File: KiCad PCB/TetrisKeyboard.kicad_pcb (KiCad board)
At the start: 2 copper layers, 100 x 94 mm, 23 parts, among them SW1 SW_Cherry_MX_1.00u_PCB, SW10 SW_Cherry_MX_1.00u_PCB, SW2 SW_Cherry_MX_1.00u_PCB, SW3 SW_Cherry_MX_1.00u_PCB, SW4 SW_Cherry_MX_1.00u_PCB, SW5 SW_Cherry_MX_1.00u_PCB, SW6 SW_Cherry_MX_1.00u_PCB, SW7 SW_Cherry_MX_1.00u_PCB, SW8 SW_Cherry_MX_1.00u_PCB, SW9 SW_Cherry_MX_1.00u_PCB

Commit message: Update file structure and pcb
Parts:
- D10, D6, D7, D8, D9: moved to F.Cu
- moved D10 3.85 mm to (96.0, 119.8)
- moved D9 2.88 mm to (51.4, 105.6)
- moved D7 2.72 mm to (57.0, 105.6)
- moved D8 2.72 mm to (62.6, 105.6)
- moved D6 2.56 mm to (68.0, 105.6)
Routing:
- net Row2-B: track 231.0 -> 215.6 mm, vias 1 -> 0

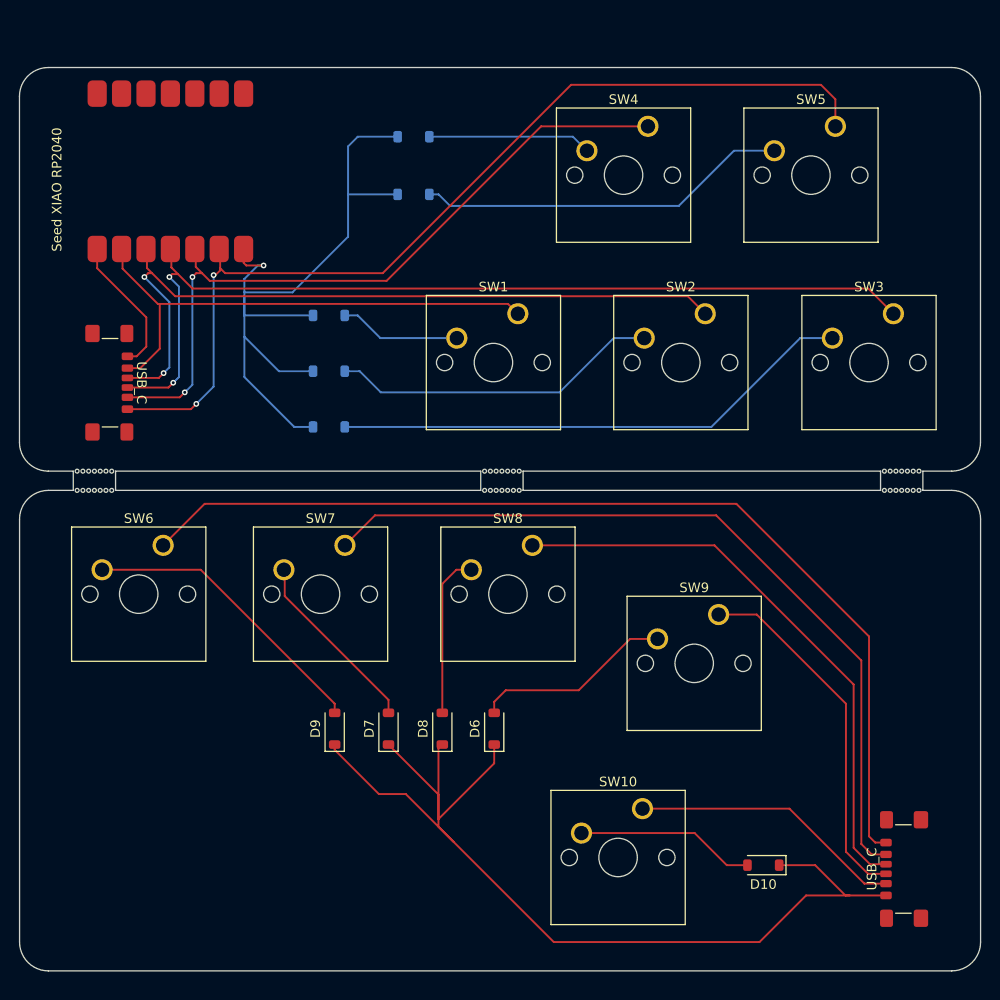
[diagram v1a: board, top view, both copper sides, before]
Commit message: Change to hot-swappable sockets, added mounting holes
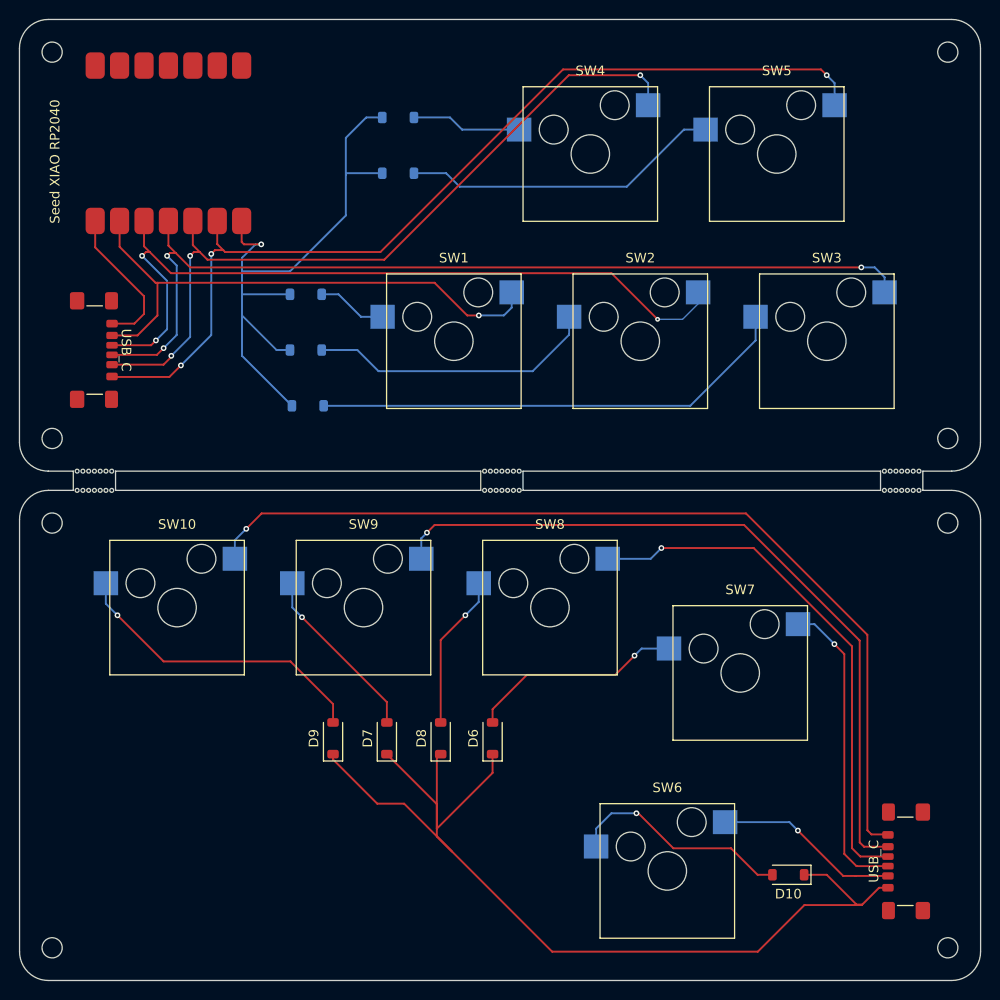
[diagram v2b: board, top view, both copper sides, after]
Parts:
- added 2.1mm: MountingHole_2.1mm, MountingHole:MountingHole_2.1mm, F.Cu at (22.0, 128.4)
- added 2.1mm: MountingHole_2.1mm, MountingHole:MountingHole_2.1mm, F.Cu at (115.2, 128.4)
- added 2.1mm: MountingHole_2.1mm, MountingHole:MountingHole_2.1mm, F.Cu at (115.2, 35.2)
- added 2.1mm: MountingHole_2.1mm, MountingHole:MountingHole_2.1mm, F.Cu at (22.0, 84.2)
- added 2.1mm: MountingHole_2.1mm, MountingHole:MountingHole_2.1mm, F.Cu at (22.0, 35.2)
- added 2.1mm: MountingHole_2.1mm, MountingHole:MountingHole_2.1mm, F.Cu at (22.0, 75.4)
- added REF**: MountingHole_2.1mm, MountingHole:MountingHole_2.1mm, F.Cu at (115.2, 84.2)
- added REF**: MountingHole_2.1mm, MountingHole:MountingHole_2.1mm, F.Cu at (115.2, 75.4)
- SW1, SW10, SW2, SW3, SW4, SW5, SW6, SW7, SW8, SW9: value SW_Cherry_MX_1.00u_PCB -> CherryMX_1.00u_KailhSocket; footprint Button_Switch_Keyboard:SW_Cherry_MX_1.00u_PCB -> CherryMX_KailhSocket:CherryMX_1.00u_KailhSocket
- moved SW6 62.5 mm to (86.0, 120.4)
- moved SW10 52.8 mm to (35.0, 93.0)
- moved SW7 43.2 mm to (93.6, 99.8)
- moved SW9 37.0 mm to (54.4, 93.0)
- moved SW3 7.50 mm to (102.6, 65.3)
- moved SW2 7.34 mm to (83.2, 65.3)
- moved SW1 7.25 mm to (63.8, 65.3)
- moved SW5 6.75 mm to (97.4, 45.8)
- moved SW8 6.73 mm to (73.8, 93.0)
- moved SW4 6.66 mm to (78.0, 45.8)
- moved USB_C 3.76 mm to (25.2, 66.2)
- moved D1 3.26 mm to (48.4, 60.4)
- moved D2 3.26 mm to (48.4, 66.2)
- moved D3 3.11 mm to (48.6, 72.0)
- moved Seed XIAO RP2040 2.92 mm to (44.6, 53.6)
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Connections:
- SW1 pad 1: Col1 -> Row1
- SW1 pad 2: Row1 -> Col1
- SW10 pad 1: Col1-B -> Row2-B
- SW10 pad 2: Row2-B -> Col5-B
- SW2 pad 1: Col2 -> Row1
- SW2 pad 2: Row1 -> Col2
- SW3 pad 1: Col3 -> Row1
- SW3 pad 2: Row1 -> Col3
- SW4 pad 1: Col4 -> Row1
- SW4 pad 2: Row1 -> Col4
- SW5 pad 1: Col5 -> Row1
- SW5 pad 2: Row1 -> Col5
- SW6 pad 1: Col5-B -> Row2-B
- SW6 pad 2: Row2-B -> Col1-B
- SW7 pad 1: Col4-B -> Row2-B
- SW7 pad 2: Row2-B -> Col2-B
- SW8 pad 1: Col3-B -> Row2-B
- SW8 pad 2: Row2-B -> Col3-B
- SW9 pad 1: Col2-B -> Row2-B
- SW9 pad 2: Row2-B -> Col4-B
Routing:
- net Row1: track 233.9 -> 200.1 mm
- net Col1-B: track 28.6 -> 19.3 mm, vias 0 -> 1
- net Col5-B: track 103.8 -> 96.8 mm, vias 0 -> 1
- net Col4-B: track 83.4 -> 77.4 mm, vias 0 -> 1
- net Col2-B: track 37.6 -> 32.0 mm, vias 0 -> 1
- net Col3-B: track 60.5 -> 55.2 mm, vias 0 -> 1
- net Col4: track 75.0 -> 80.2 mm, vias 2 -> 3
- net Row2-B: track 215.6 -> 220.3 mm, vias 0 -> 5
- net Col1: track 53.1 -> 57.4 mm, vias 0 -> 1
- net Col2: track 77.4 -> 81.4 mm, vias 2 -> 3
- net Col3: track 95.8 -> 97.3 mm, vias 2 -> 3
- net Row2: track 14.7 -> 15.5 mm
- net Col5: track 99.5 -> 99.8 mm, vias 2 -> 3
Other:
- board size 100 x 94 mm -> 100 x 100 mm
